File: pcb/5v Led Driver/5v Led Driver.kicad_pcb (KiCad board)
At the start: 2 copper layers, 43 parts, among them J1 USB_C_Receptacle_USB2.0_16P, J2 Conn_01x02_Pin, J3 Conn_01x02_Pin, J4 Conn_01x03_Pin, J5 Conn_01x02_Pin, SW2 PTS815 SJM 250 SMTR LFS, U1 RP2040, U2 W25Q16JVUXIQ TR, U3 RT6150B-33GQW, Y1 ABM8G-12.000MHZ-B4Y-T

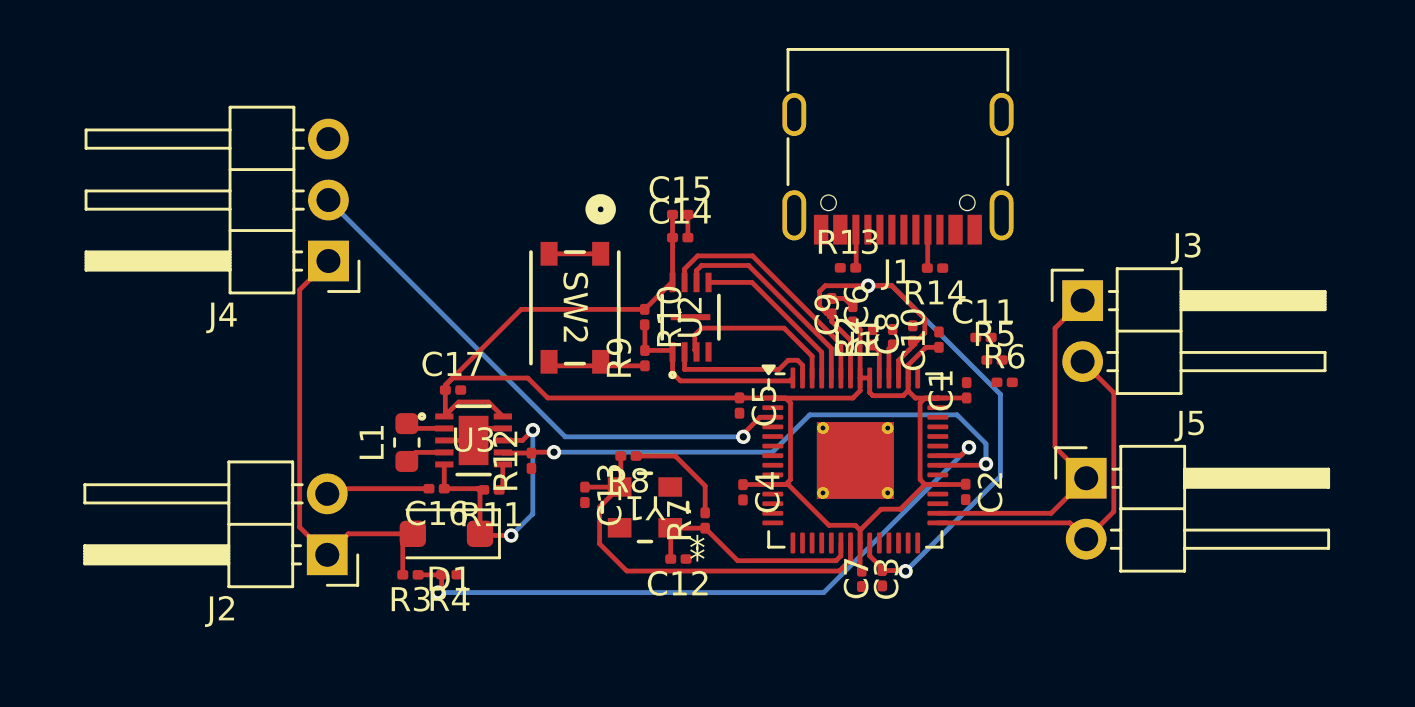
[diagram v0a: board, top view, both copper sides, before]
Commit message: cant access pwmRead
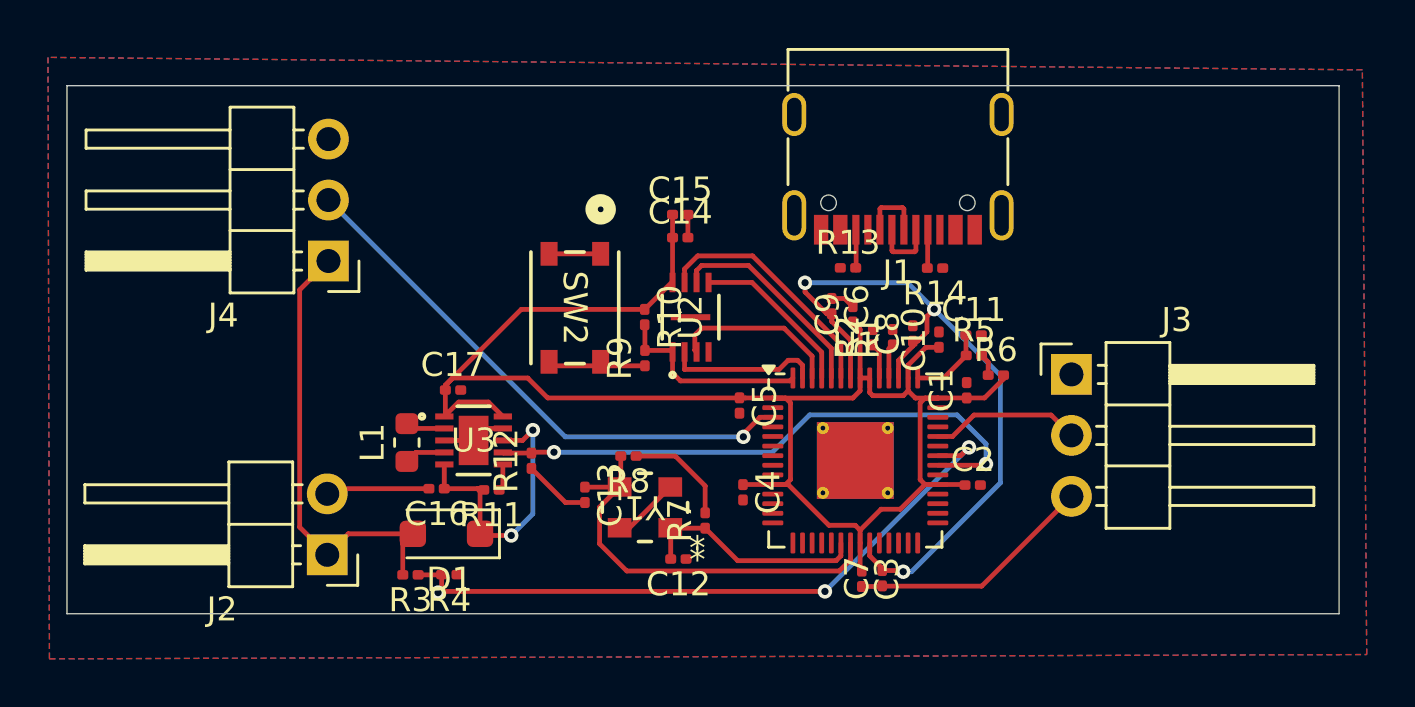
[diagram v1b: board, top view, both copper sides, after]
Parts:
- removed J5: Conn_01x02_Pin, Connector_PinHeader_2.54mm:PinHeader_1x02_P2.54mm_Horizontal
- J3: value Conn_01x02_Pin -> Conn_01x03_Pin; footprint Connector_PinHeader_2.54mm:PinHeader_1x02_P2.54mm_Horizontal -> Connector_PinHeader_2.54mm:PinHeader_1x03_P2.54mm_Horizontal
- moved J3 3.11 mm to (133.6, 86.9)
- moved R5 0.88 mm to (129.5, 86.1)
- moved R6 0.47 mm to (130.4, 86.9)
- moved C11 0.42 mm to (129.5, 85.2)
- moved C2 0.41 mm to (129.5, 91.5), turned to 0 degrees
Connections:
- J3 pad 1: /I2C D+ -> unconnected-(J3-Pin_1-Pad1)
- J3 pad 2: /I2C D- -> /PWM IN
- U1 pad 29: /I2C D- -> unconnected-(U1-GPIO18-Pad29)
- U1 pad 30: /I2C D+ -> unconnected-(U1-GPIO19-Pad30)
- U1 pad 38: unconnected-(U1-GPIO26/ADC0-Pad38) -> /PWM IN
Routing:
- net GND: track 11.1 -> 27.0 mm
- net /I2C D+: track 15.2 -> 0.00 mm
- net /I2C D-: track 14.9 -> 0.00 mm
- net /PWM IN: track 0.00 -> 6.29 mm
- net /ADC_AVDD: track 0.00 -> 3.26 mm
- net /D-: track 0.00 -> 2.78 mm
- net /D+: track 0.00 -> 2.78 mm
- net /3V3: track 68.9 -> 71.0 mm
- net /ADC_VREF: track 0.00 -> 0.93 mm
- net /1V1: track 30.9 -> 30.5 mm, vias 2 -> 3
- net /GPIO24: track 27.8 -> 27.9 mm, vias 2 -> 3
- added copper zone on B.Cu, net GND
- added copper zone on F.Cu, net GND
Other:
- board outline added: 53 x 22 mm

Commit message: good
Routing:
- net GND: track 27.0 -> 45.3 mm, vias 0 -> 58
- net /D+: track 2.78 -> 7.06 mm
- net /D-: track 2.78 -> 6.95 mm

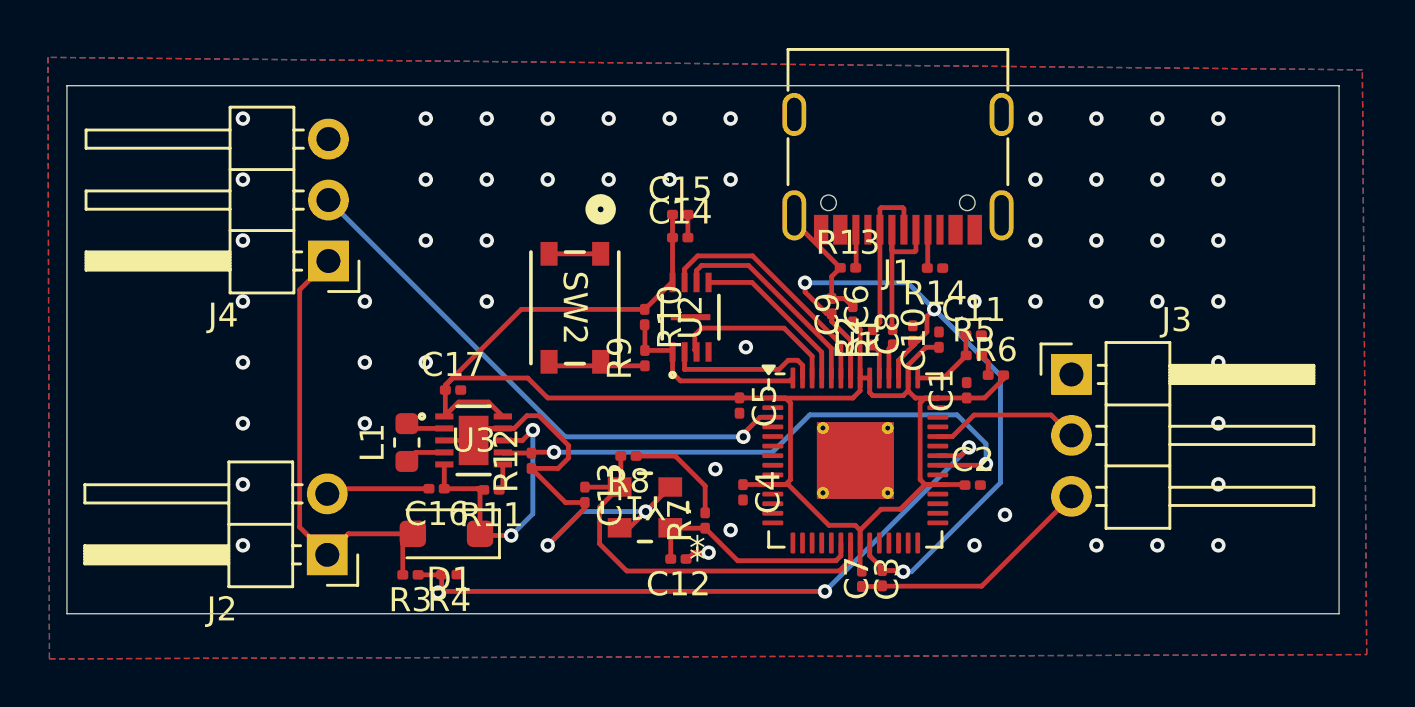
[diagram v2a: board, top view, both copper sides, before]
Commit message: usbc mabye not good
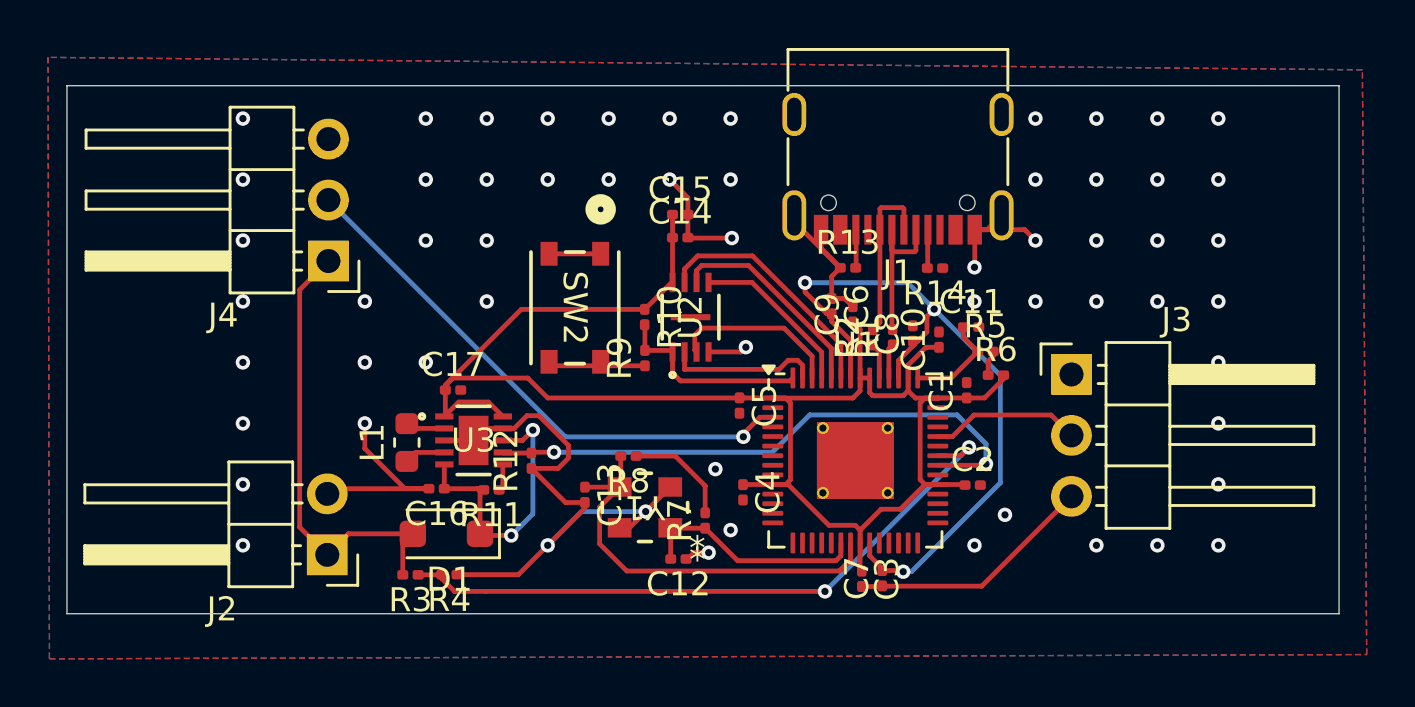
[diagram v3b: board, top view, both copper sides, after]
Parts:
- moved R5 0.51 mm to (130.0, 85.9)
- moved C11 0.35 mm to (129.4, 84.9)
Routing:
- net GND: track 45.3 -> 66.8 mm, vias 58 -> 60
- net /ADC_AVDD: track 3.26 -> 4.22 mm
- net /GPIO24: track 27.9 -> 27.3 mm, vias 3 -> 2
